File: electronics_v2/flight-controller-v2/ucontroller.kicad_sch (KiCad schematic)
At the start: 46 parts

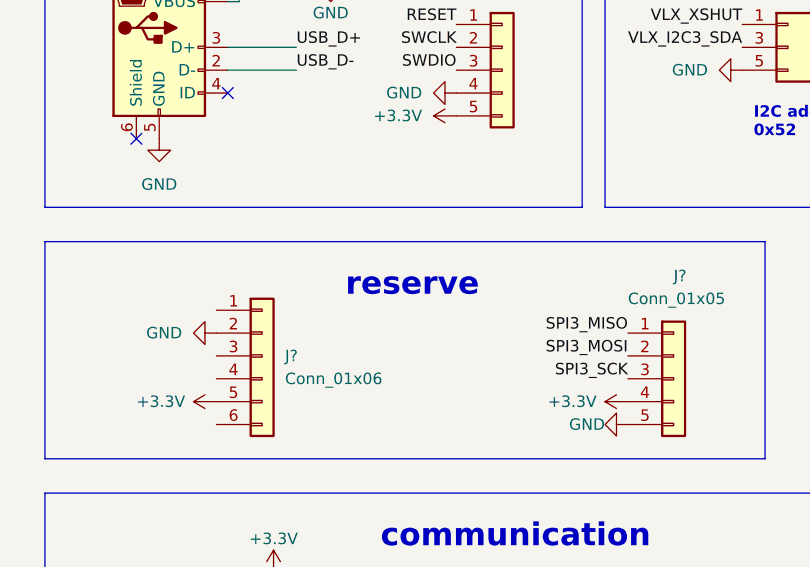
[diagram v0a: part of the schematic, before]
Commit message: develop Hall velocity sense circuit
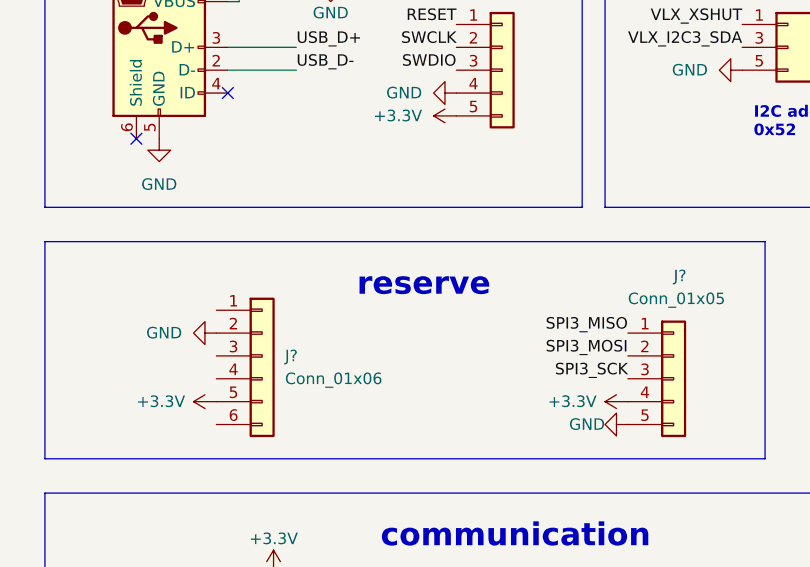
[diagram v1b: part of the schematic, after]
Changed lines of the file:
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@@
     (effects (font (size 1.27 1.27) (thickness 0.254) bold) (justify left bottom))
   )
-  (text "reserve" (at 226.06 67.31 180)
+  (text "reserve" (at 227.33 67.31 180)
     (effects (font (size 2.54 2.54) (thickness 0.508) bold) (justify right bottom))
   )

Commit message: FC scheme complete
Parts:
- added D3, D4: LED, LED_SMD:LED_0603_1608Metric, symbol Device:LED
- added R17, R18: 1k, Resistor_SMD:R_0603_1608Metric, symbol Device:R
- J3: renamed from J?; footprint (none) -> Connector_IDC:IDC-Header_2x03_P2.54mm_Vertical
- J5: renamed from J?; footprint (none) -> goose:tht_pin_01x06
- JP1, JP2, JP3, JP4, JP5: renamed from JP?; footprint (none) -> goose:tht_pin_01x02
- SW1, SW2: renamed from SW?; footprint Button_Switch_SMD:SW_Push_1P1T_NO_CK_KMR2 -> Button_Switch_SMD:SW_SPST_FSMSM
- SW3, SW4: renamed from SW?; footprint Button_Switch_SMD:SW_Push_SPST_NO_Alps_SKRK -> Button_Switch_SMD:SW_SPST_FSMSM
- gave numbers to parts that had none: 35
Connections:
- net GND: now also D3.1 (K), D4.1 (K)
- net I_SENSE: now also U2.25 (PC5); no longer U2.21 (PA5)
- net V_SENSE: now also U2.24 (PC4); no longer U2.20 (PA4)
- net PA0: now reaches J5.1 (Pin_1)
- net PA0: now also U2.14 (PA0)
- net UART2_TX: now reaches J5.3 (Pin_3)
- net UART2_TX: now also U2.16 (PA2)
- net UART2_RX: now reaches J5.4 (Pin_4)
- net UART2_RX: now also U2.17 (PA3)
- net PA1: now reaches J5.6 (Pin_6)
- net PA1: now also U2.15 (PA1)
- net LED_G: now reaches U2.33 (PB12)
- net LED_G: now also R18.2
- net LED_R: now reaches U2.34 (PB13)
- net LED_R: now also R17.2
- net LED_TIM2_CH3 renamed LED_B
- net SWO: no longer names the net of U2.55 (PB3)
- new net: D3.2 (A), R17.1
- new net: D4.2 (A), R18.1
- new net HALL_TIM2_ETR: U2.21 (PA5)
- no-connect marks 35 -> 29
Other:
- moved on the sheet: D5, R13, R19

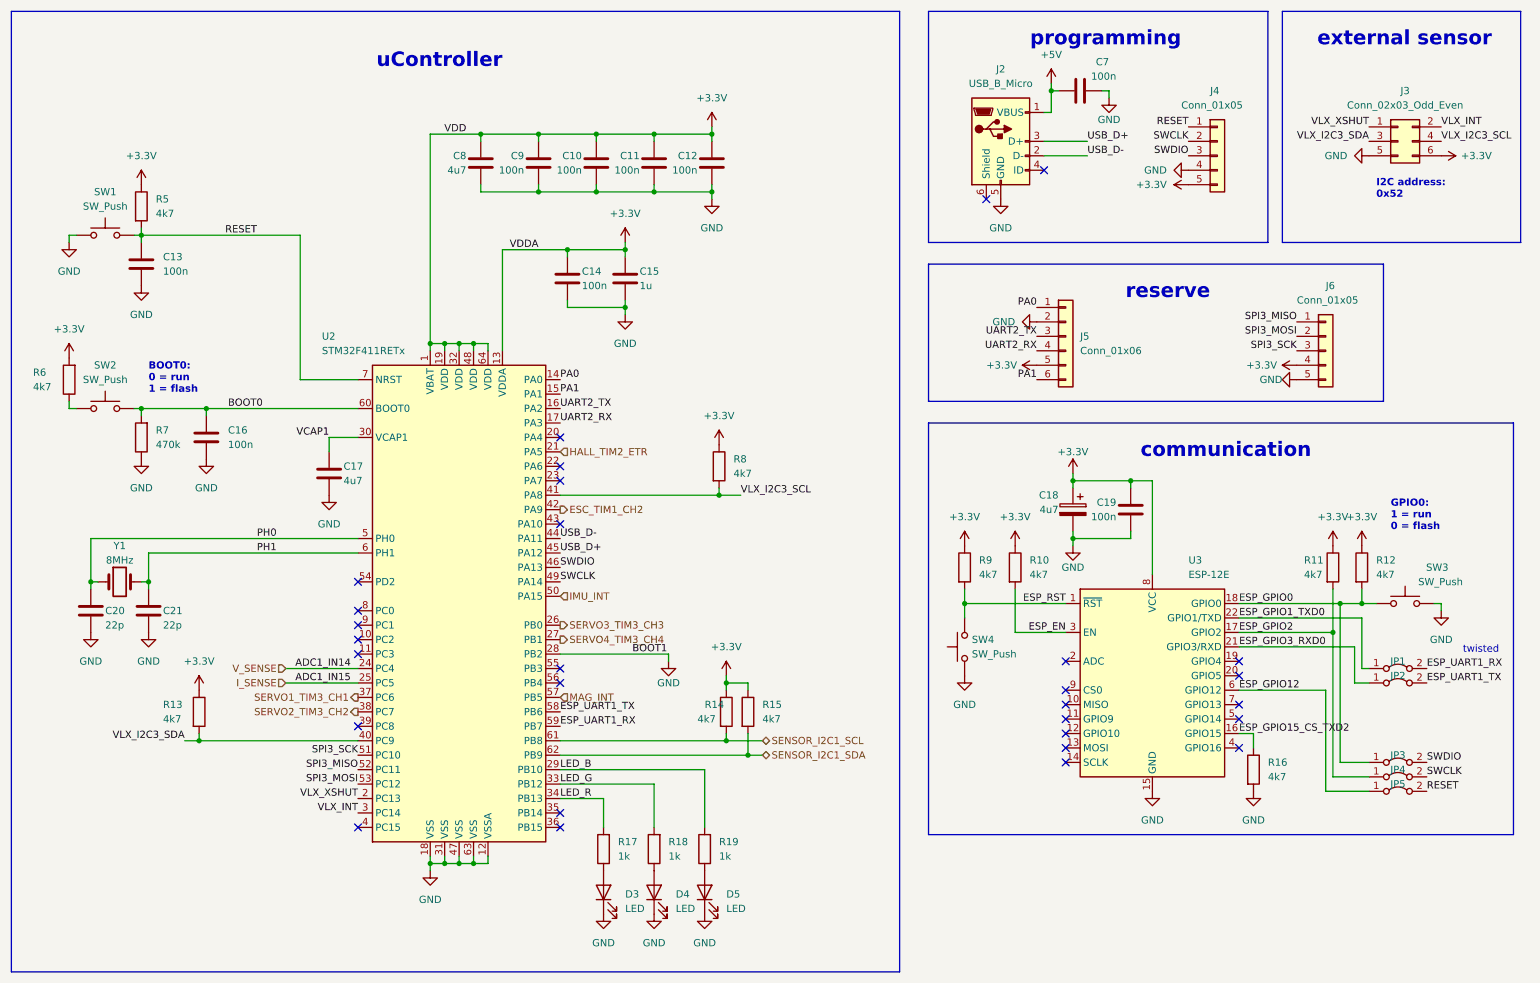
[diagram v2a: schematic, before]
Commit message: first board cutout and layout
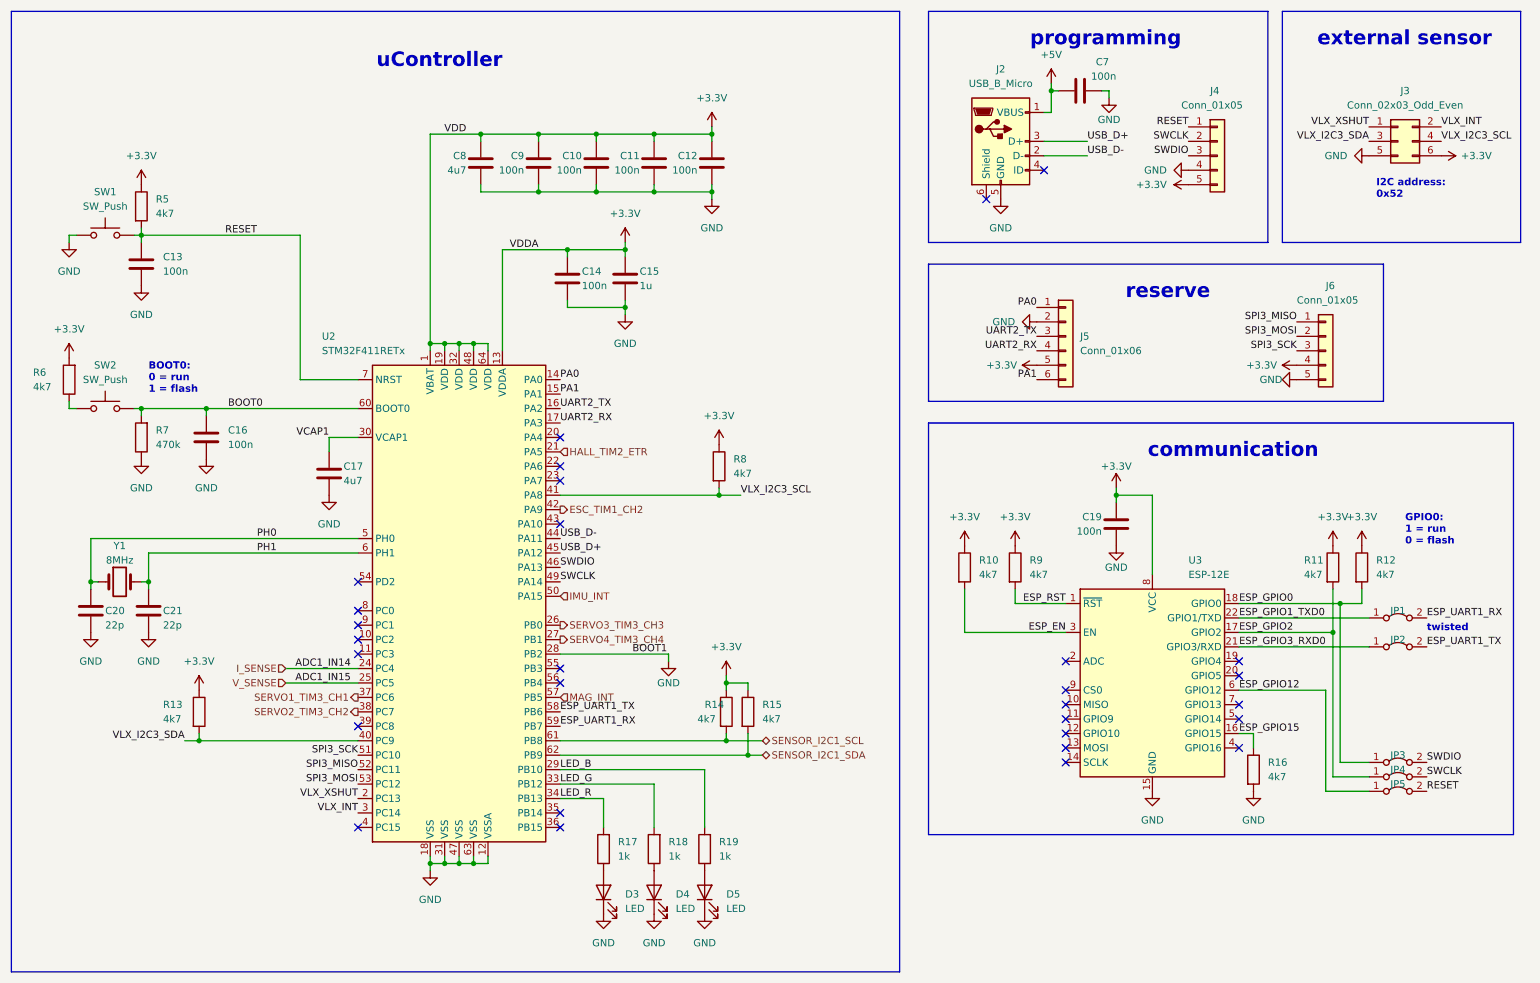
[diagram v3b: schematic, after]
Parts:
- removed C18: 4u7, Capacitor_Tantalum_SMD:CP_EIA-3216-18_Kemet-A, symbol Device:C_Polarized
- removed SW3, SW4: SW_Push, Button_Switch_SMD:SW_SPST_FSMSM, symbol Switch:SW_Push
- JP1, JP2, JP3, JP4, JP5: footprint goose:tht_pin_01x02 -> Jumper:SolderJumper-2_P1.3mm_Open_TrianglePad1.0x1.5mm
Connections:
- net I_SENSE: now also U2.24 (PC4); no longer U2.25 (PC5)
- net V_SENSE: now also U2.25 (PC5); no longer U2.24 (PC4)
- net ESP_GPIO15_CS_TXD2 renamed ESP_GPIO15
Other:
- moved on the sheet: C19, JP1, JP2, R10, R9

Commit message: edge XT60 connector & INA226 I2C measurement
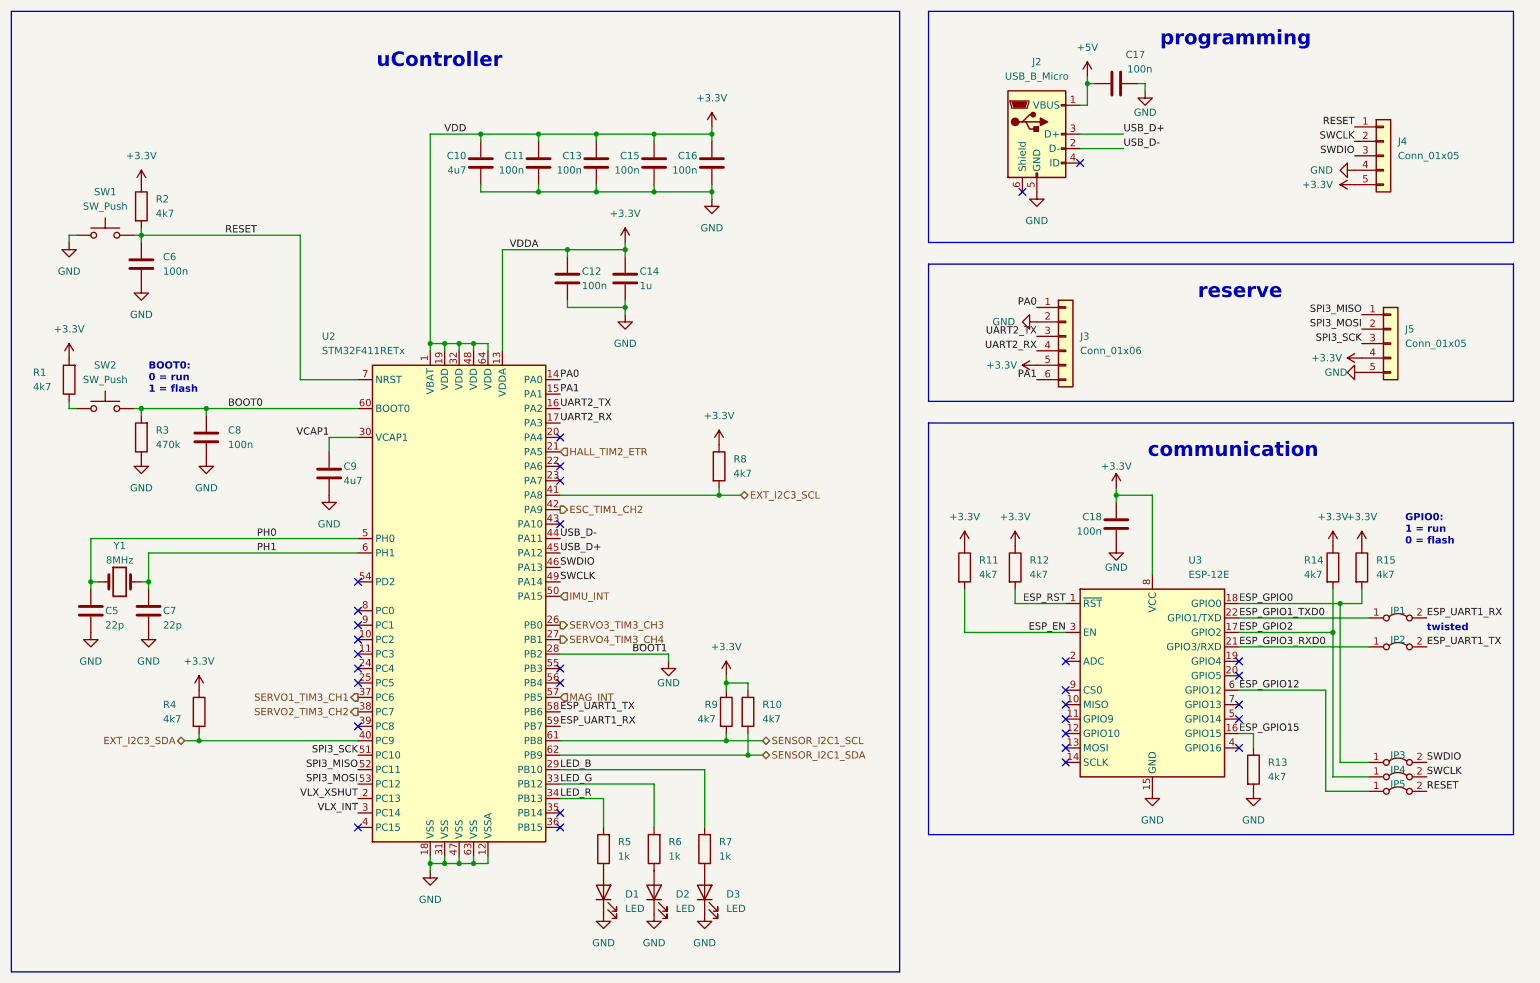
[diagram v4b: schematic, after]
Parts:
- removed J3: Conn_02x03_Odd_Even, Connector_IDC:IDC-Header_2x03_P2.54mm_Vertical, symbol Connector_Generic:Conn_02x03_Odd_Even
- renumbered C8 to C10, C9 to C11, C14 to C12, C10 to C13, C15 to C14, C11 to C15, C12 to C16, C7 to C17, C19 to C18, C20 to C5, C13 to C6, C21 to C7, C16 to C8, C17 to C9, D3 to D1, D4 to D2, D5 to D3, J5 to J3, J6 to J5, R6 to R1, R15 to R10, R10 to R11, R9 to R12, R16 to R13, R11 to R14, R12 to R15, R5 to R2, R7 to R3, R13 to R4, R17 to R5, R18 to R6, R19 to R7, R14 to R9
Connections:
- net I_SENSE: no longer names the net of U2.24 (PC4)
- net VLX_I2C3_SCL renamed EXT_I2C3_SCL
- net VLX_I2C3_SDA renamed EXT_I2C3_SDA
- net V_SENSE: no longer names the net of U2.25 (PC5)
- no-connect marks 29 -> 31
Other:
- note removed: "I2C address: 0x52"
- note removed: "external sensor"
- moved on the sheet: C17, J2, J4, J5

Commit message: move PLI to FC
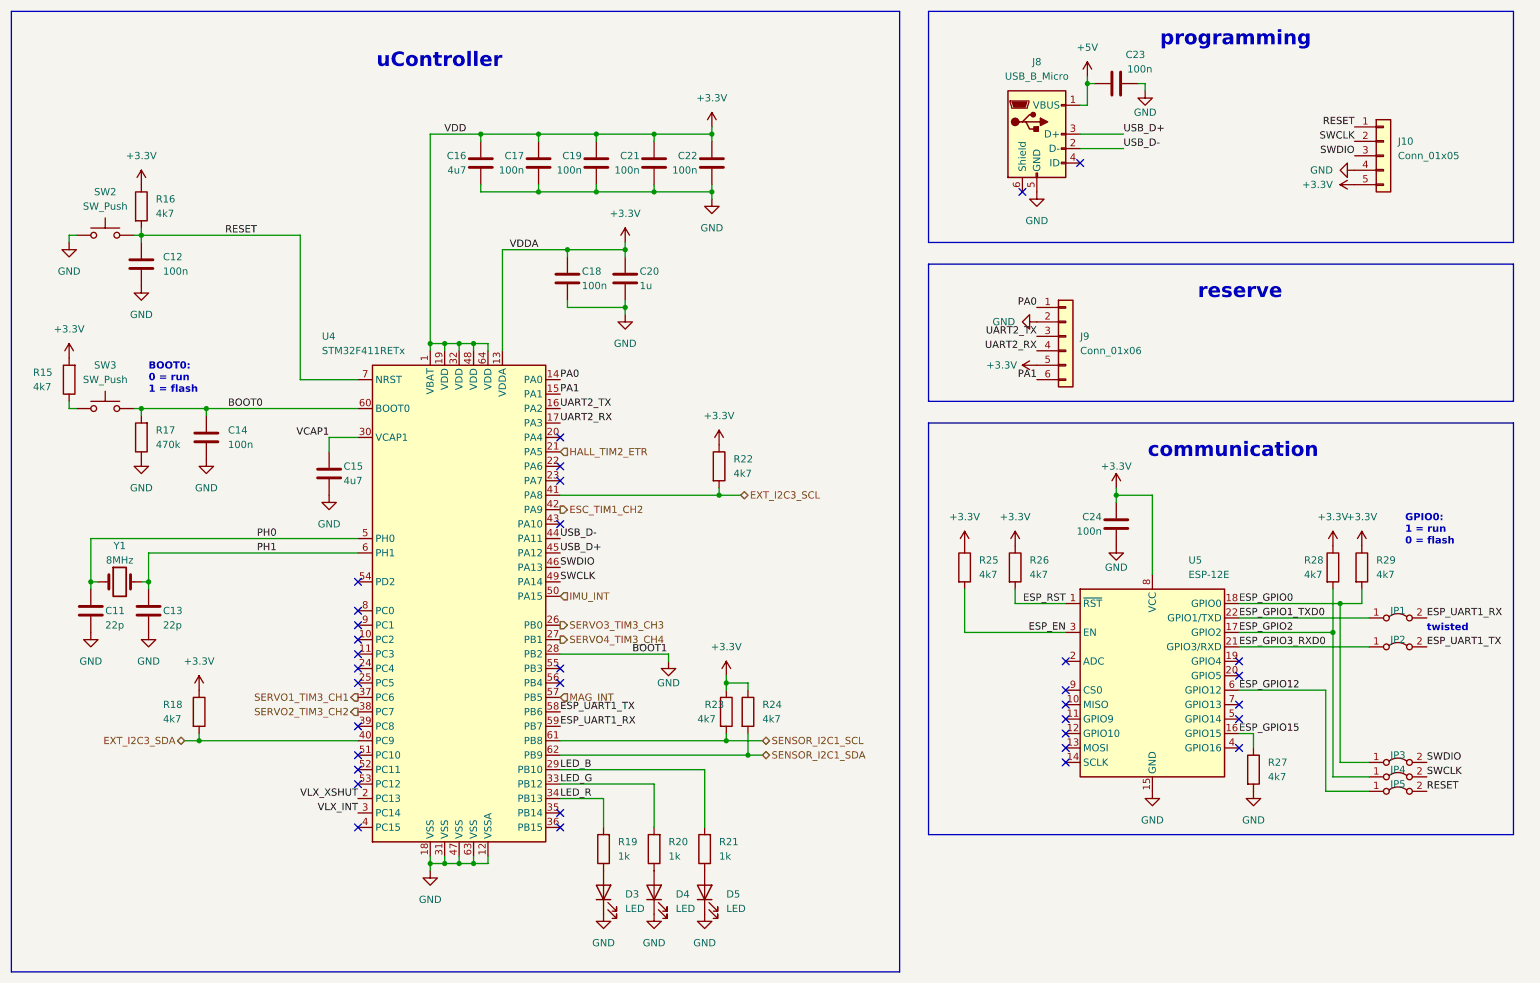
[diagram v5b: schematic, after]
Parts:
- removed J5: Conn_01x05, goose:tht_pin_01x05, symbol Connector_Generic:Conn_01x05
- renumbered C5 to C11, C6 to C12, C7 to C13, C8 to C14, C9 to C15, C10 to C16, C11 to C17, C12 to C18, C13 to C19, C14 to C20, C15 to C21, C16 to C22, C17 to C23, C18 to C24, D1 to D3, D2 to D4, D3 to D5, J4 to J10, J2 to J8, J3 to J9, R1 to R15, R2 to R16, R3 to R17, R4 to R18, R5 to R19, R6 to R20, R7 to R21, R8 to R22, R9 to R23, R10 to R24, R11 to R25, R12 to R26, R13 to R27, R14 to R28, R15 to R29, SW1 to SW2, SW2 to SW3, U2 to U4, U3 to U5
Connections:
- net SPI3_MISO: no longer names the net of U4.52 (PC11)
- net SPI3_MOSI: no longer names the net of U4.53 (PC12)
- net SPI3_SCK: no longer names the net of U4.51 (PC10)
- no-connect marks 31 -> 34

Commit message: fix route names
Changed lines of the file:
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@@
-    (effects (font (size 1.27 1.27)) (justify right bottom))
-  )
-  (label "VLX_XSHUT" (at 77.47 154.94 180)
     (effects (font (size 1.27 1.27)) (justify right bottom))
   )
@@
   (label "SWDIO" (at 265.43 148.59 0)
     (effects (font (size 1.27 1.27)) (justify left bottom))
-  )
-  (label "VLX_INT" (at 77.47 157.48 180)
-    (effects (font (size 1.27 1.27)) (justify right bottom))
   )
   (label "ESP_EN" (at 201.93 125.73 180)
@@
     (effects (font (size 1.27 1.27)) (justify left))
   )
+  (hierarchical_label "VLX_XSHUT" (shape output) (at 77.47 154.94 180)
+    (effects (font (size 1.27 1.27)) (justify right))
+  )
+  (hierarchical_label "VLX_INT" (shape input) (at 77.47 157.48 180)
+    (effects (font (size 1.27 1.27)) (justify right))
+  )
   (symbol (lib_id "Device:R") (at 39.37 50.8 0) (unit 1)
